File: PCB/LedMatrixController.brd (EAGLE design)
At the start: 104 x 50 mm, 17 parts, among them IC1 AT90S2313S, IC2 74LS595D

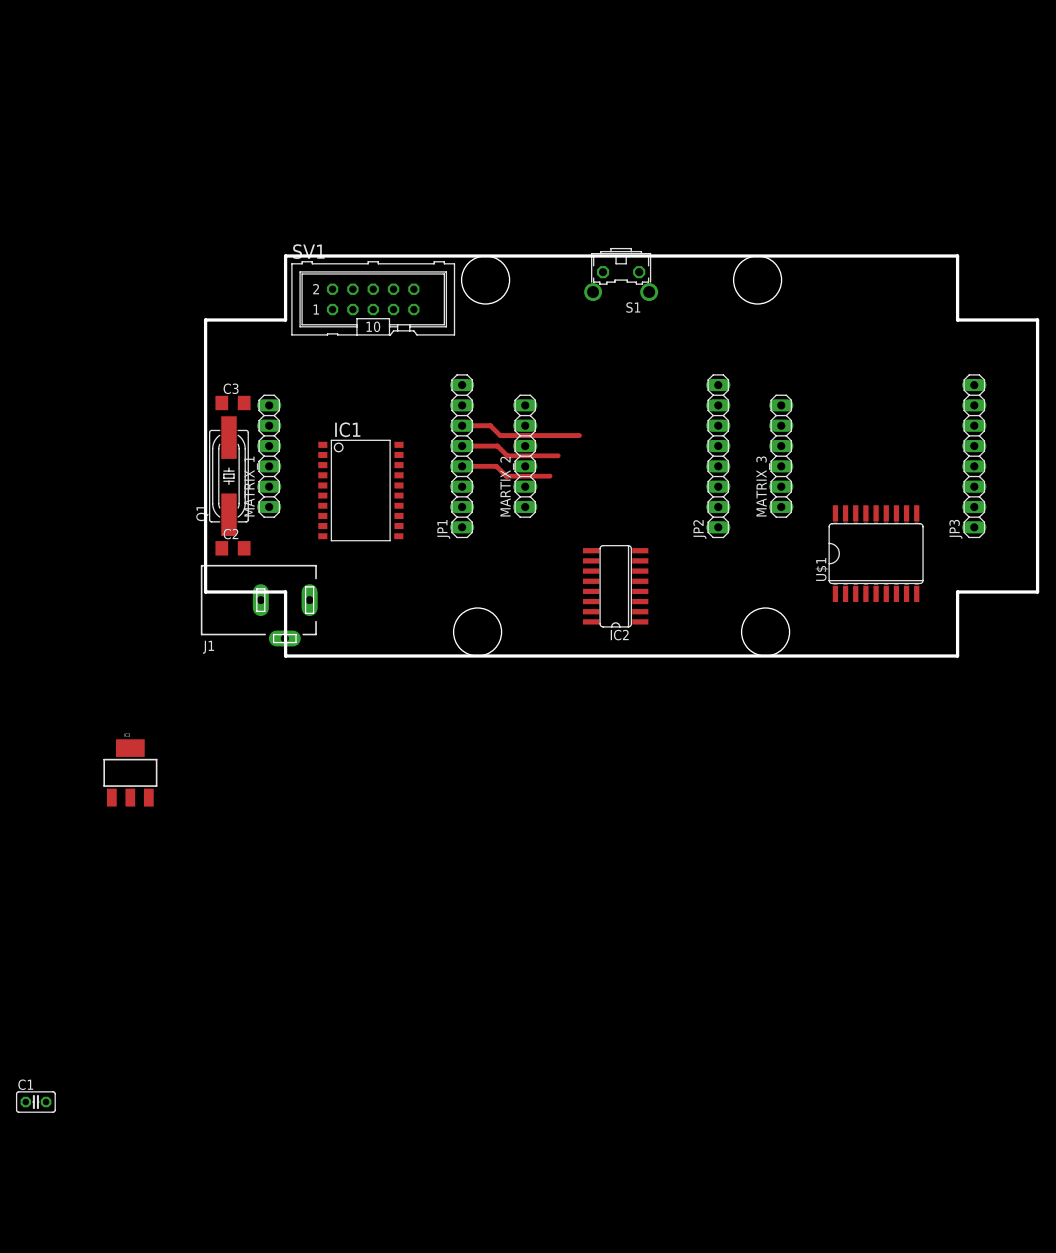
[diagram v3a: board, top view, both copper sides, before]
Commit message: Improvments in the top layer of matrix controller pcb. Added eeprom, connected power source and almost all IC.
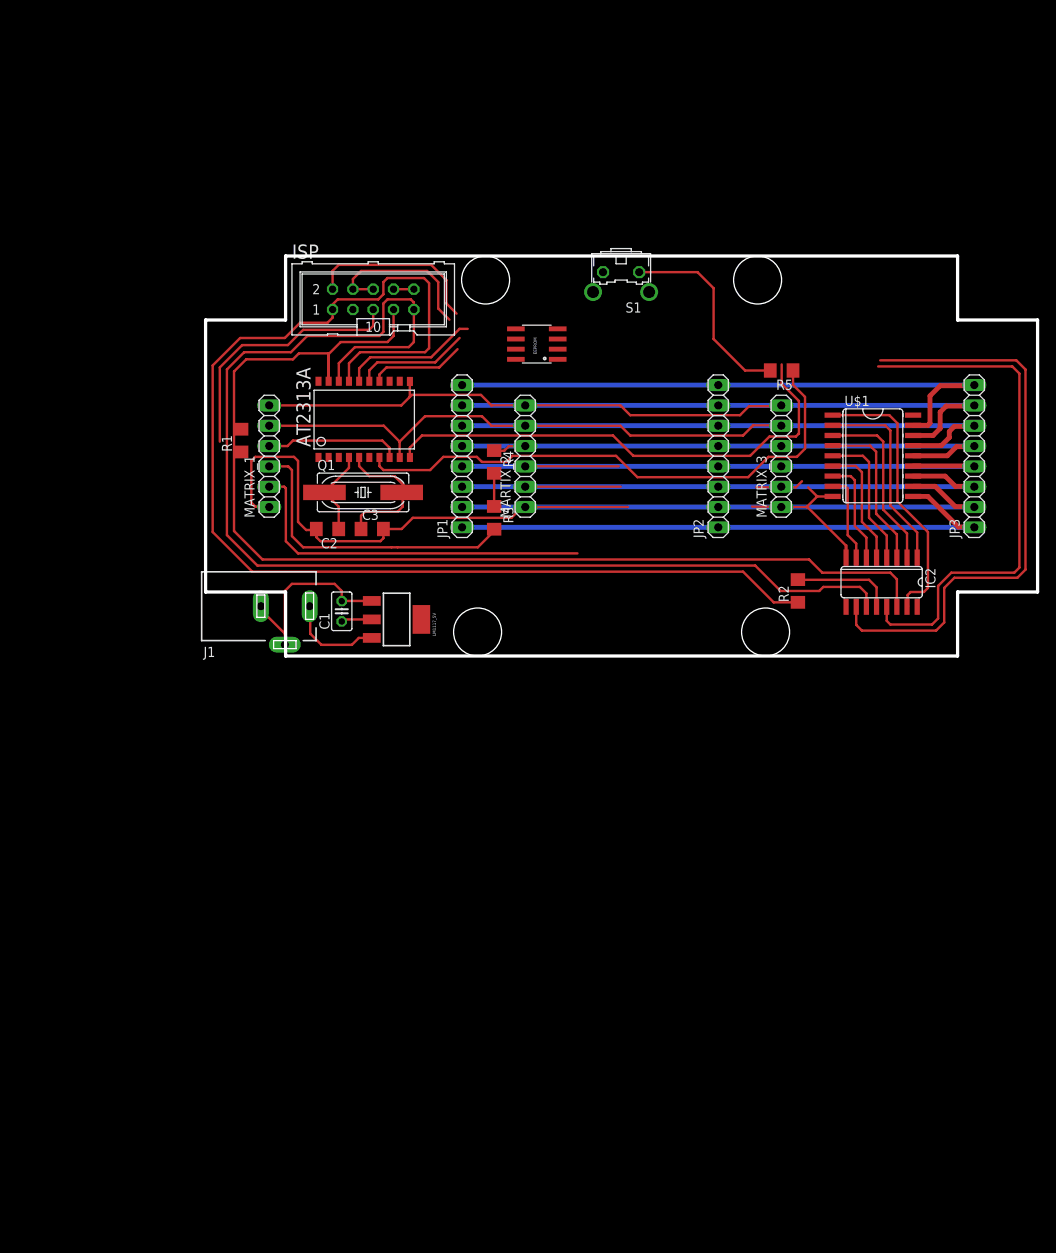
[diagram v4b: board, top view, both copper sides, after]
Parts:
- removed IC1: AT90S2313S, atmel:SO20L
- removed IC3: (no value), SparkFun-PowerIC:SOT223
- added AT2313A: AT90S2313S, atmel:SO20L
- added EEPROM: AT24C08, MJ:SO08
- added LM1117_5V: (no value), SparkFun-PowerIC:SOT223
- added R1, R2, R3, R4, R5: 0R, resistor:R1206
- moved C1 72.3 mm to (17.0, 5.59), turned to 90 degrees
- moved IC2 33.2 mm to (84.5, 9.23), turned to 180 degrees
- moved C3 23.5 mm to (20.8, 15.9)
- moved Q1 16.9 mm to (19.7, 20.4), turned to 0 degrees
- moved U$1 12.2 mm to (83.4, 25.0), turned to 270 degrees
- moved C2 12.1 mm to (15.2, 15.9), turned to 180 degrees
- moved J1 0.76 mm to (9.91, 6.22)
- renumbered SV1 to ISP
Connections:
- removed net OUT: MARTIX_2.4, MATRIX_1.3
- new net COL_OUT: MATRIX_1.3, R3.2
- new net N$10: AT2313A.15, EEPROM.6
- new net N$11: R3.1, R4.2
- new net N$12: AT2313A.14, EEPROM.7
- new net N$13: AT2313A.1, R1.1
- new net N$14: R5.2, S1.1
- new net N$6: AT2313A.16, EEPROM.5
- new net N$7: MARTIX_2.4, R4.1
- new net N$9: ISP.5, R1.2
- new net ROW_LATCH: AT2313A.17, ISP.1, R2.1
- new net ROW_SCK: AT2313A.18, IC2.11, ISP.9
- new net ROW_SERIAL_DATA: AT2313A.19, IC2.14, ISP.7
- new net VCC: AT2313A.20, C1.1, EEPROM.8, IC2.10, ISP.2, LM1117_5V.2, LM1117_5V.4, MARTIX_2.2, MATRIX_1.2, MATRIX_3.2, U$1.18
- net +5V: no longer C1.1, IC1.20, IC3.2, IC3.4, MARTIX_2.2, MATRIX_1.2, MATRIX_3.2
- net COL_CLK: now also AT2313A.9; no longer IC1.11
- net COL_CLR: now also AT2313A.11; no longer IC1.8
- net COL_DATA: now also AT2313A.8; no longer IC1.9
- net GND: now also AT2313A.10, EEPROM.1, EEPROM.2, EEPROM.3, EEPROM.4, IC2.13, ISP.10, ISP.4, ISP.6, ISP.8, LM1117_5V.1; no longer IC1.10, IC3.1
- net N$1: now also AT2313A.4; no longer IC1.4
- net N$2: now also LM1117_5V.3; no longer IC3.3
- net N$3: now also AT2313A.5; no longer IC1.5
- net N$4: now also AT2313A.7, R5.1; no longer IC1.7, S1.1
- net N$5: now also IC2.12, R2.2; no longer S1.2
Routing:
- net GND: track 0.00 -> 263.9 mm
- net VCC: track 0.00 -> 163.2 mm
- net ROW_SCK: track 0.00 -> 152.7 mm
- net ROW_LATCH: track 0.00 -> 152.5 mm
- net ROW_SERIAL_DATA: track 0.00 -> 140.7 mm
- net ROW8: track 0.00 -> 75.8 mm
- net ROW7: track 0.00 -> 74.4 mm
- net ROW1: track 0.00 -> 73.3 mm
- net ROW2: track 0.00 -> 72.7 mm
- net ROW3: track 0.00 -> 72.2 mm
- net COL_CLK: track 0.00 -> 69.7 mm
- net N$4: track 0.00 -> 68.7 mm
- net COL_CLR: track 0.00 -> 68.1 mm
- net ROW4: track 11.5 -> 71.8 mm
- net ROW5: track 12.5 -> 72.2 mm
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
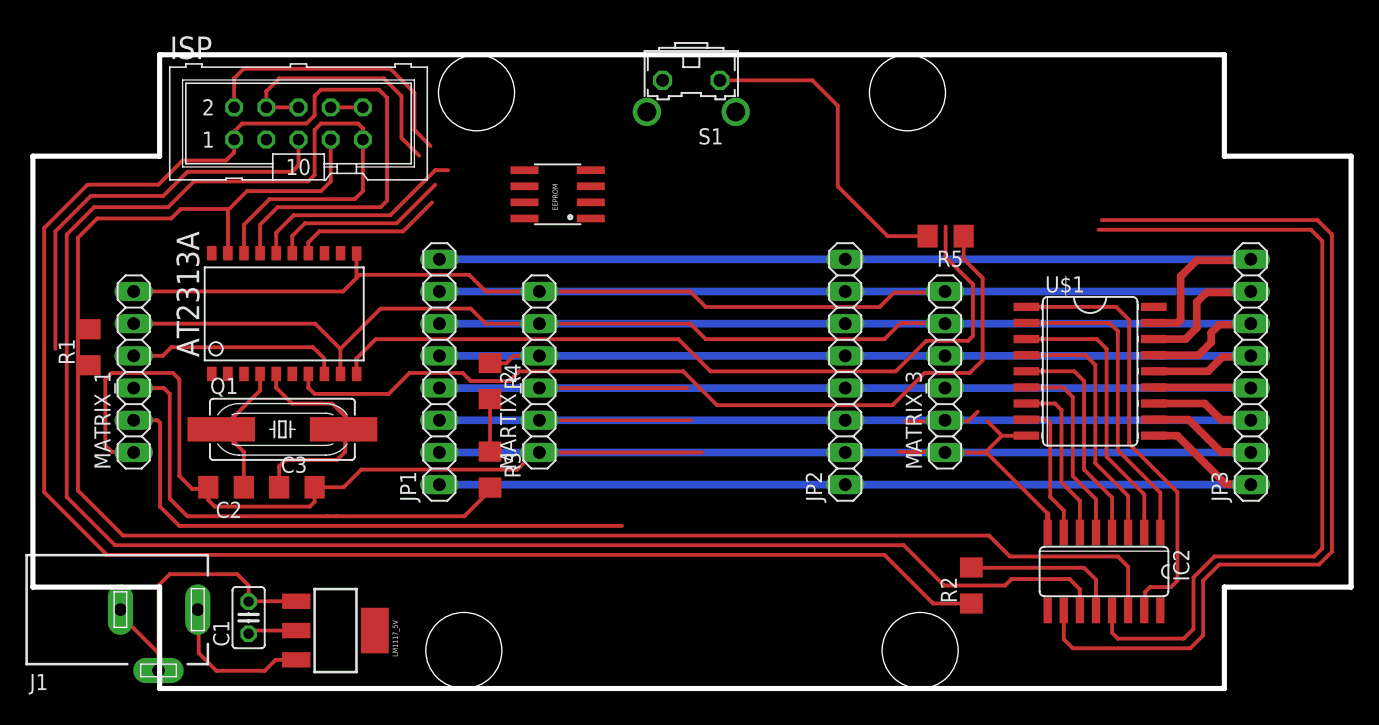
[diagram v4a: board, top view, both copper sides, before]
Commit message: Added usb connector, and power led.
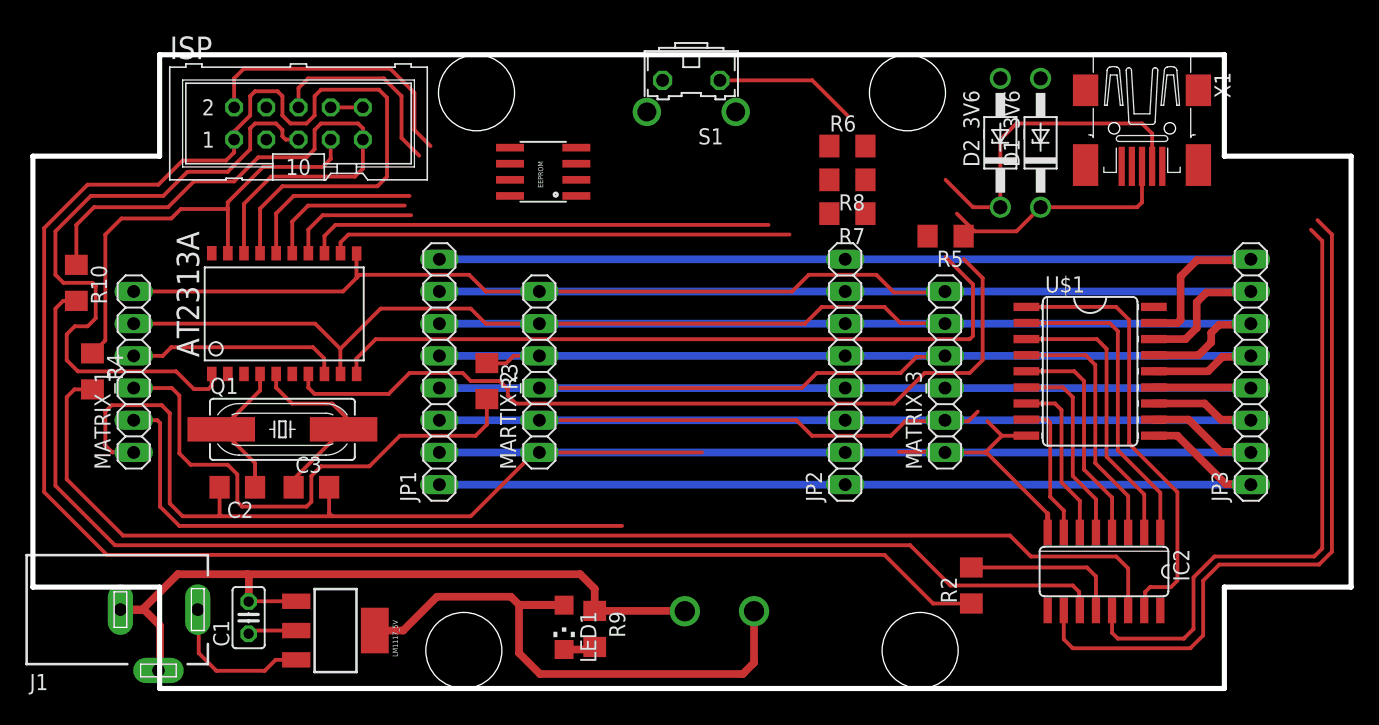
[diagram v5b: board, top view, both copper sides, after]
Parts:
- removed R1: 0R, resistor:R1206
- added D1_3V6, D2_3V6: 1N4728, diode:DO41Z10
- added LED1: (no value), led:CHIPLED_1206
- added R10, R9: 0R, resistor:R1206
- added R6: 2k2, resistor:R1206
- added R7, R8: 68R, resistor:R1206
- added X1: MINI-USB-32005-201, con-cypressindustries:32005-201
- moved R4 31.4 mm to (4.70, 25.0)
- moved R3 6.99 mm to (35.8, 24.3)
- moved EEPROM 2.11 mm to (40.3, 40.8)
- moved C3 1.14 mm to (22.0, 15.9)
- moved C2 0.89 mm to (16.1, 15.9)
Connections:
- removed net N$9: ISP.5, R1.2
- new net COL_OUT_2: MARTIX_2.4, R3.1
- new net N$17: LED1.C, R9.2
- new net USB_D+: AT2313A.12, R7.2
- new net USB_D-: AT2313A.13, R8.2
- new net USB_DATA+: D1_3V6.C, R7.1, X1.3
- new net USB_DATA-: D2_3V6.C, R6.2, R8.1, X1.2
- net GND: now also D1_3V6.A, D2_3V6.A, R9.1, X1.5
- net N$11: now also IC2.11, R10.2; no longer R3.1, R4.2
- net N$13: now also ISP.5; no longer R1.1
- net N$7: now also IC2.14, R4.2; no longer MARTIX_2.4, R4.1
- net ROW_SCK: now also R10.1; no longer IC2.11
- net ROW_SERIAL_DATA: now also R4.1; no longer IC2.14
- net VCC: now also LED1.A, R6.1, X1.1
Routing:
- net ROW_SERIAL_DATA: track 140.7 -> 35.8 mm
- net ROW_SCK: track 152.7 -> 47.7 mm
- net N$11: track 4.14 -> 101.6 mm
- net N$7: track 4.14 -> 98.7 mm
- net N$13: track 0.00 -> 52.3 mm
- net VCC: track 163.2 -> 211.3 mm, vias 0 -> 1
- net USB_D-: track 0.00 -> 36.8 mm
- net USB_D+: track 0.00 -> 36.5 mm
- net N$9: track 32.6 -> 0.00 mm
- net USB_DATA-: track 0.00 -> 26.0 mm
- net N$8: track 11.8 -> 32.9 mm
- net USB_DATA+: track 0.00 -> 19.0 mm
- net N$14: track 25.2 -> 11.6 mm
- net GND: track 263.9 -> 276.0 mm, vias 0 -> 1
- net COL_OUT_2: track 0.00 -> 4.40 mm
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
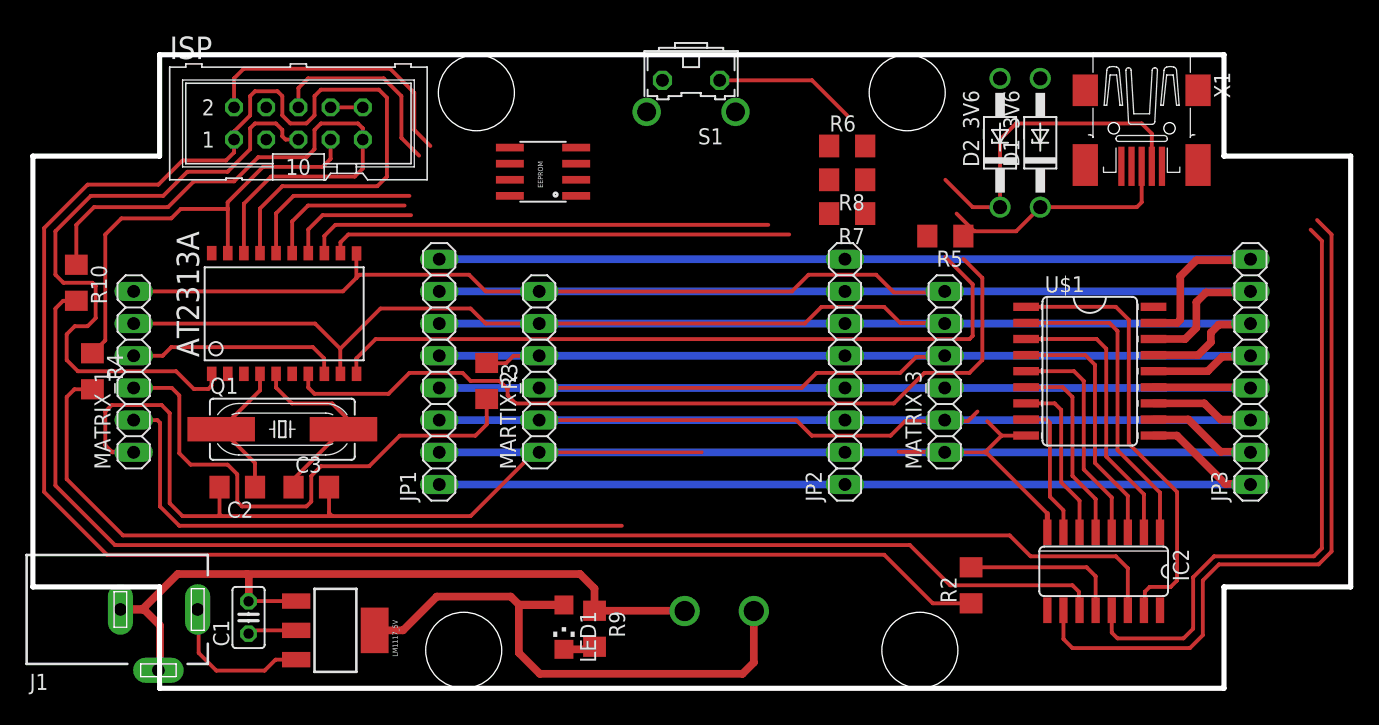
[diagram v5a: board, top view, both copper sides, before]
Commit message: Finished first version of the led matrix controller pcb
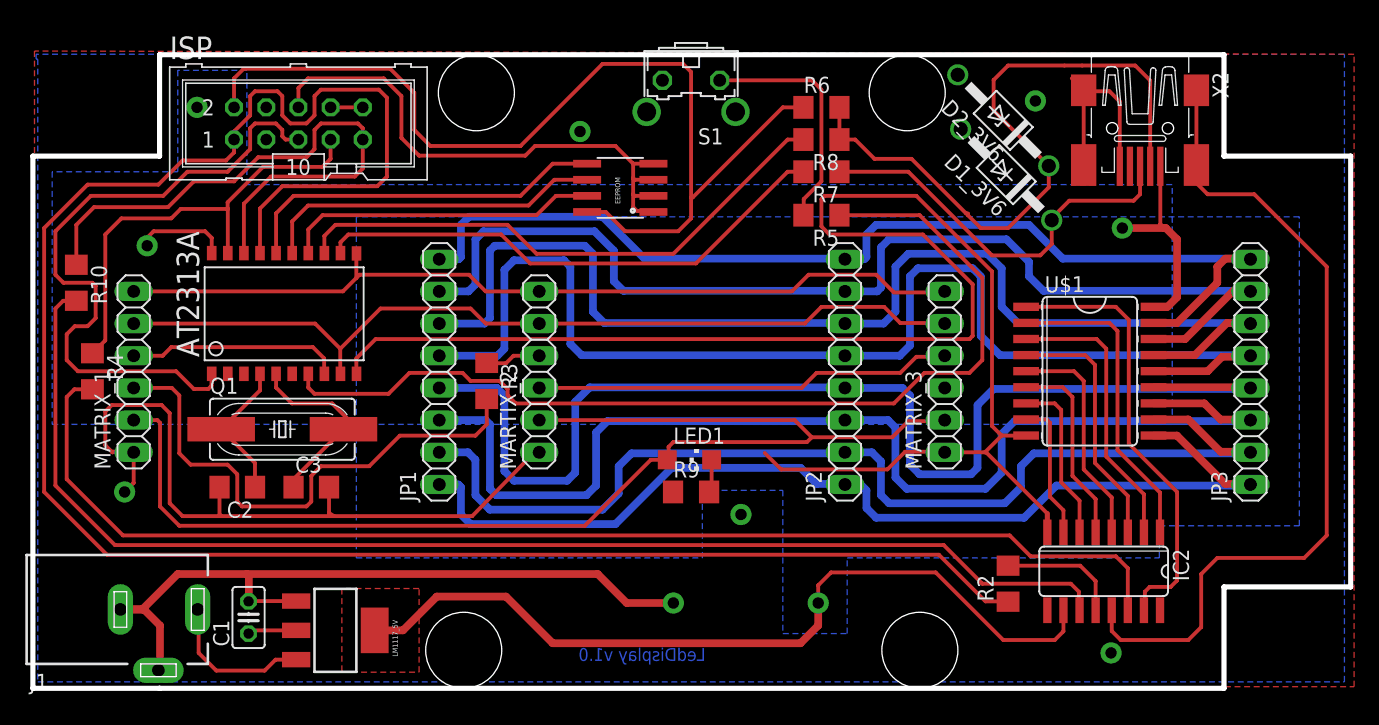
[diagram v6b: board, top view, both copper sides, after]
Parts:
- removed X1: MINI-USB-32005-201, con-cypressindustries:32005-201
- added X2: MINI-USB-SCHIELD-32005-201, con-cypressindustries:32005-201
- moved LED1 16.5 mm to (51.8, 18.0), turned to 270 degrees
- moved R9 13.2 mm to (51.9, 15.5), turned to 0 degrees
- moved R5 9.92 mm to (62.2, 37.3)
- moved EEPROM 6.23 mm to (46.4, 39.5)
- moved R7 3.88 mm to (62.2, 40.8)
- moved R8 3.77 mm to (62.2, 43.3)
- moved D1_3V6 3.68 mm to (76.8, 40.5), turned to 135 degrees
- moved R6 3.66 mm to (62.2, 45.8)
- moved R2 2.92 mm to (77.0, 8.26)
- moved D2_3V6 1.79 mm to (76.6, 44.8), turned to 135 degrees
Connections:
- net GND: now also S1.2, X2.5, X2.M1, X2.M2, X2.M3, X2.M4; no longer X1.5
- net USB_DATA+: now also X2.3; no longer X1.3
- net USB_DATA-: now also X2.2; no longer X1.2
- net VCC: now also X2.1; no longer X1.1
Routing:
- net GND: track 276.0 -> 375.9 mm, vias 1 -> 6
- net VCC: track 211.3 -> 269.0 mm, vias 1 -> 4
- net USB_DATA-: track 26.0 -> 53.9 mm
- net ROW5: track 72.2 -> 97.3 mm
- net ROW4: track 71.8 -> 96.4 mm
- net ROW3: track 72.2 -> 91.3 mm
- net ROW6: track 73.2 -> 92.1 mm
- net N$10: track 11.9 -> 27.1 mm
- net N$6: track 14.2 -> 29.3 mm
- net N$12: track 10.4 -> 25.0 mm
- net USB_DATA+: track 19.0 -> 31.9 mm
- net ROW2: track 72.7 -> 85.3 mm
- net ROW7: track 74.4 -> 86.7 mm
- net N$4: track 66.5 -> 77.7 mm
- net ROW1: track 73.3 -> 81.4 mm
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- added copper zone on layer 1, net GND
- added copper zone on layer 16, net GND
- added copper zone on layer 1, net VCC
- added copper zone on layer 16, net VCC
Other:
- outline, holes or cut-outs redrawn
- board text added: "LedDisplay v1.0"

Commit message: ULN2803 has been replaced with NPN transistors
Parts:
- removed U$1: ULN2803A, MJ:SO18W
- added T1, T2, T3, T4, T5, T6, T7, T8: BC817-40SMD, transistor-npn:SOT23-BEC
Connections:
- net GND: no longer U$1.9
- net R1: now also T1.B; no longer U$1.1
- net R2: now also T2.B; no longer U$1.2
- net R3: now also T3.B; no longer U$1.3
- net R4: now also T4.B; no longer U$1.4
- net R5: now also T5.B; no longer U$1.5
- net R6: now also T6.B; no longer U$1.6
- net R7: now also T7.B; no longer U$1.7
- net R8: now also T8.B; no longer U$1.8
- net ROW1: now also T1.E; no longer U$1.10
- net ROW2: now also T2.E; no longer U$1.11
- net ROW3: now also T3.E; no longer U$1.12
- net ROW4: now also T4.E; no longer U$1.13
- net ROW5: now also T5.E; no longer U$1.14
- net ROW6: now also T6.E; no longer U$1.15
- net ROW7: now also T7.E; no longer U$1.16
- net ROW8: now also T8.E; no longer U$1.17
- net VCC: now also T1.C, T2.C, T3.C, T4.C, T5.C, T6.C, T7.C, T8.C; no longer U$1.18
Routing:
- net VCC: track 269.0 -> 344.8 mm
- net GND: track 375.9 -> 313.3 mm
- net R7: track 13.2 -> 33.8 mm
- net R2: track 24.8 -> 5.90 mm
- net R5: track 17.7 -> 28.0 mm
- net R1: track 35.1 -> 26.3 mm
- net R4: track 20.1 -> 13.5 mm
- net ROW8: track 82.1 -> 88.2 mm
- net ROW7: track 86.7 -> 80.7 mm
- net ROW1: track 81.4 -> 75.3 mm
- net R8: track 11.1 -> 16.8 mm
- net ROW3: track 91.3 -> 86.2 mm
- net ROW5: track 97.3 -> 92.3 mm
- net R6: track 15.4 -> 19.3 mm
- net ROW6: track 92.1 -> 88.7 mm
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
